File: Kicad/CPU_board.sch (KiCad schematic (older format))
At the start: 2 parts

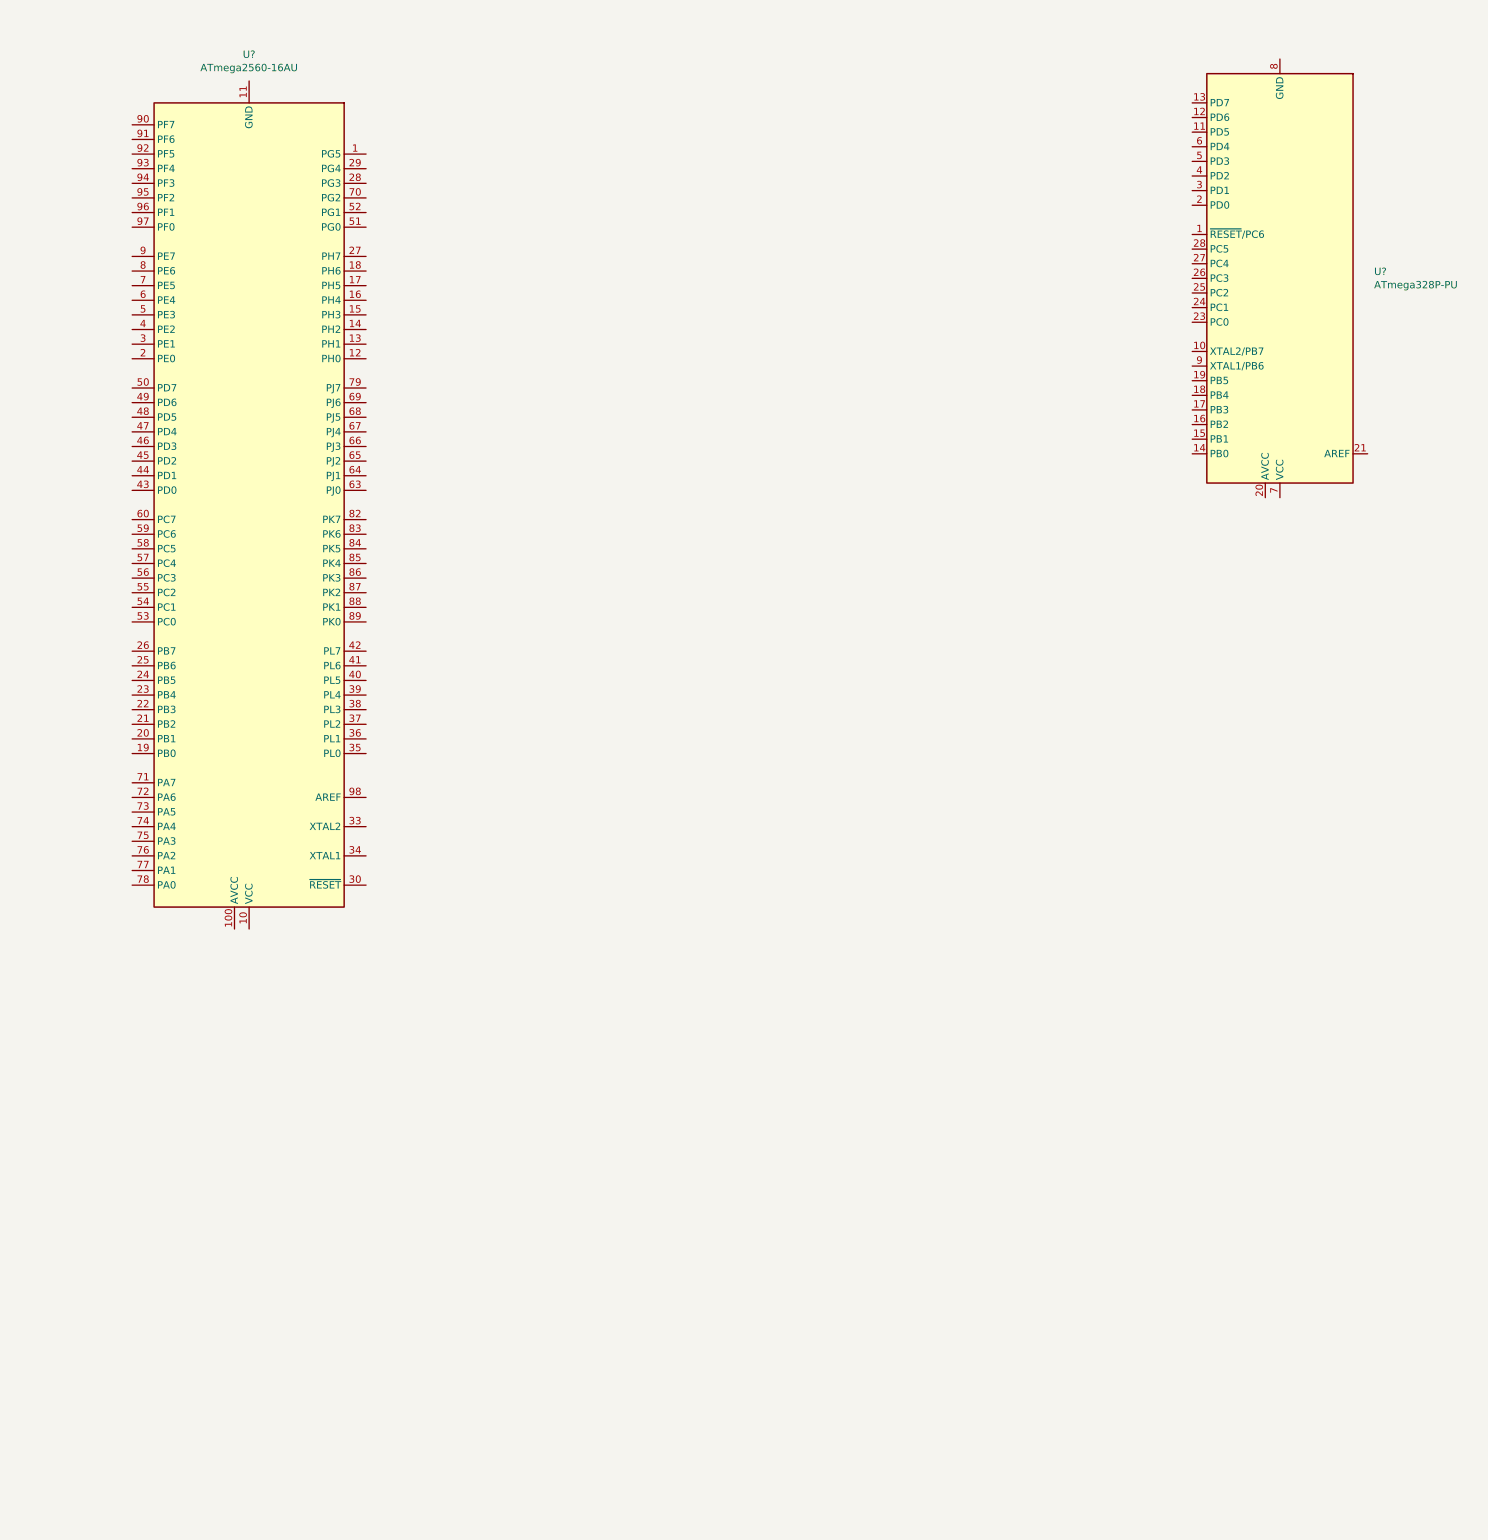
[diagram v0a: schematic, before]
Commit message: supprimé :        Kicad/CPU_board-cache.lib 	modifié :         Kicad/CPU_board.pro 	modifié :         Kicad/CPU_board.sch 	supprimé :        Kicad/CPU_board.sch-bak 	supprimé :        Kicad/Main_board-cache.lib 	modifié :         Kicad/Main_board.sch 	supprimé :        Kicad/Screen_board-cache.lib 	supprimé :        Kicad/Screen_board-rescue.dcm 	supprimé :        Kicad/Screen_board-rescue.lib 	supprimé :        Kicad/Screen_board.pro 	supprimé :        Kicad/Screen_board.sch 	supprimé :        Kicad/Screen_board.sch-bak
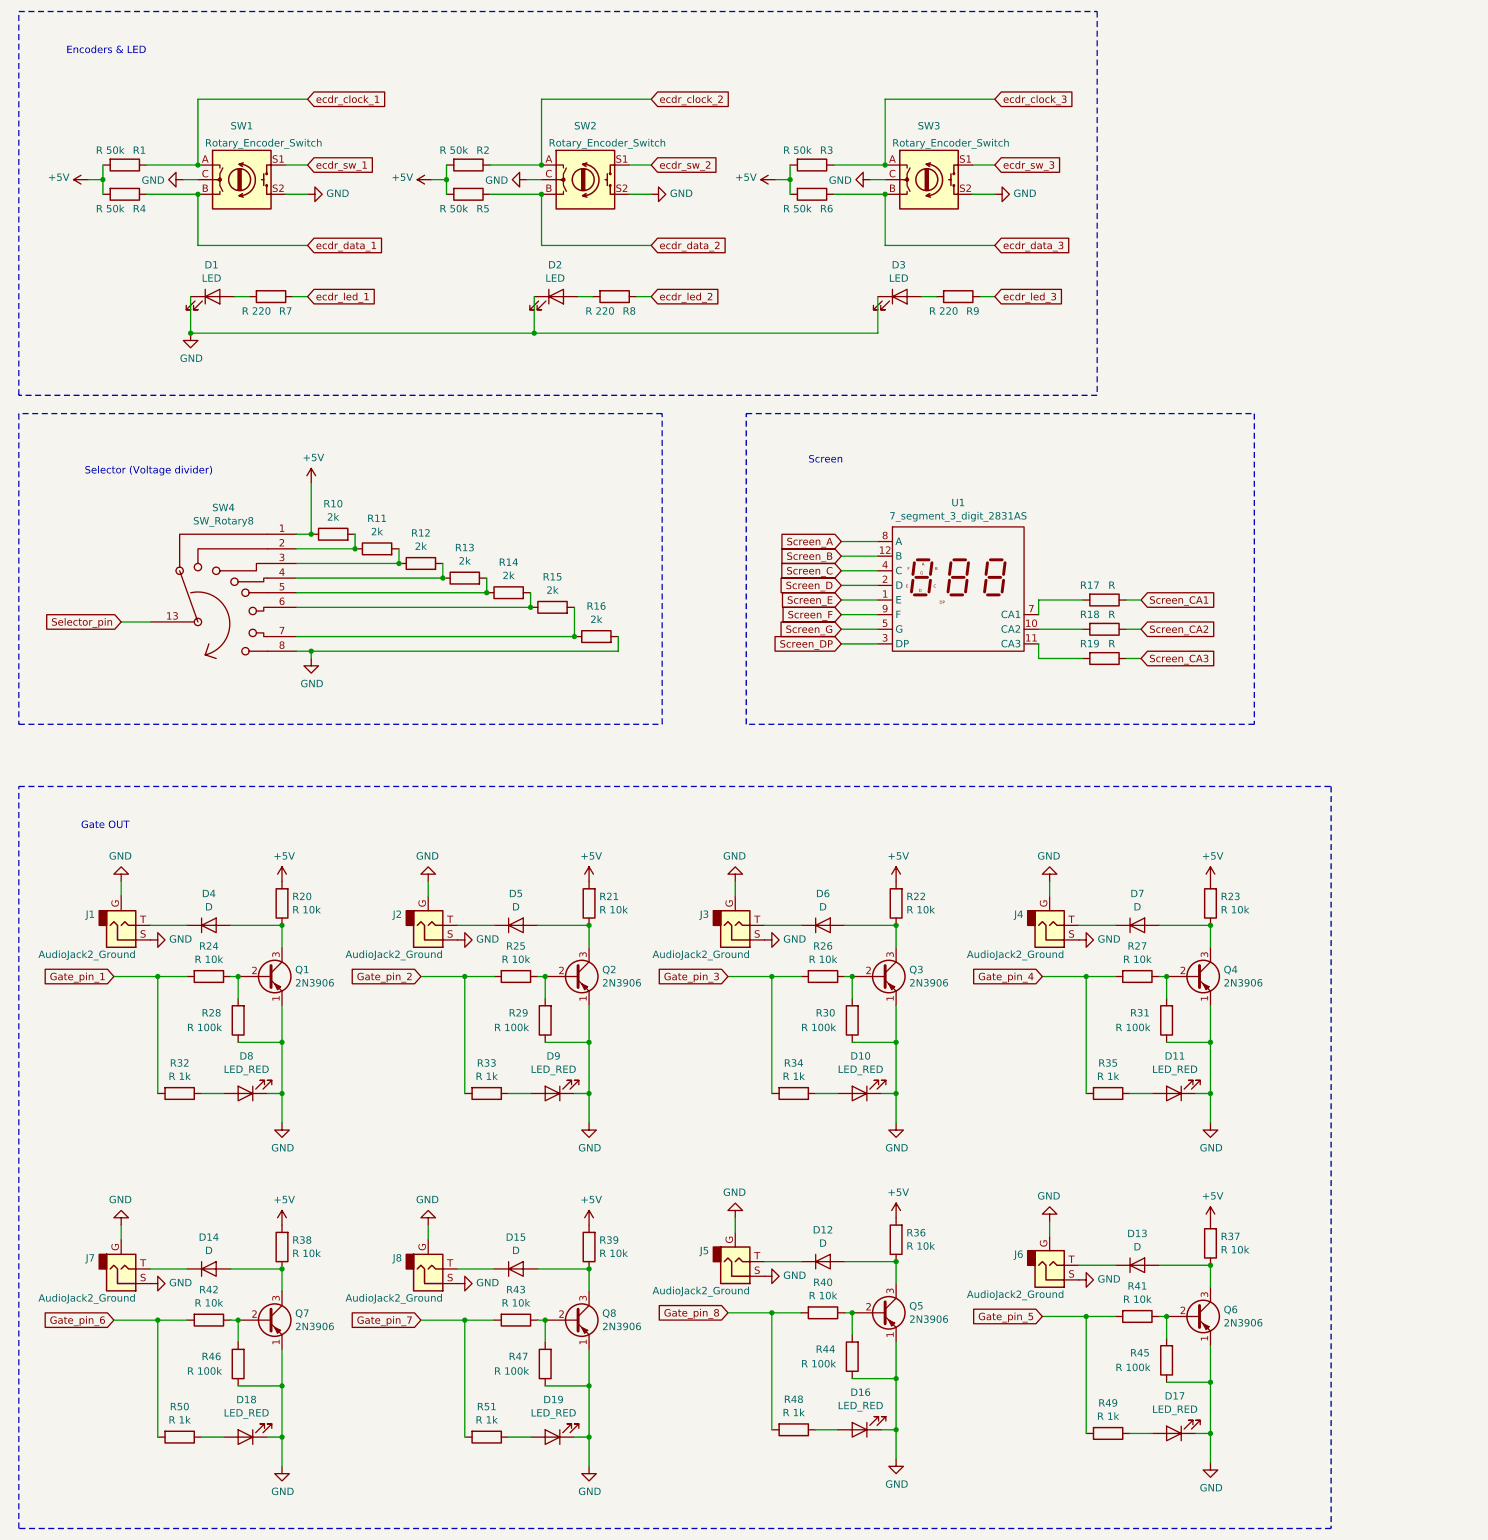
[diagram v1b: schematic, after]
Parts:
- removed U?: ATmega328P-PU, Package_DIP:DIP-28_W7.62mm, symbol MCU_Microchip_ATmega:ATmega328P-PU
- removed U?: ATmega2560-16AU, Package_QFP:TQFP-100_14x14mm_P0.5mm, symbol MCU_Microchip_ATmega:ATmega2560-16AU
- added D1, D2, D3: LED, symbol Device:LED
- added D10, D11, D16, D17, D18, D19, D8, D9: LED_RED, symbol Device:LED
- added D12, D13, D14, D15, D4, D5, D6, D7: D, symbol Device:D
- added J1, J2, J3, J4, J5, J6, J7, J8: AudioJack2_Ground, symbol Connector:AudioJack2_Ground
- added Q1, Q2, Q3, Q4, Q5, Q6, Q7, Q8: 2N3906, Package_TO_SOT_THT:TO-92_Inline, symbol Transistor_BJT:2N3906
- added R1, R2, R3, R4, R5, R6: R 50k, symbol Device:R
- added R10, R11, R12, R13, R14, R15, R16: 2k, symbol Device:R
- added R17, R18, R19: R, symbol Device:R
- added R20, R21, R22, R23, R24, R25, R26, R27, R36, R37, R38, R39, R40, R41, R42, R43: R 10k, symbol Device:R
- added R28, R29, R30, R31, R44, R45, R46, R47: R 100k, symbol Device:R
- added R32, R33, R34, R35, R48, R49, R50, R51: R 1k, symbol Device:R
- added R7, R8, R9: R 220, symbol Device:R
- added SW1, SW2, SW3: Rotary_Encoder_Switch, symbol Device:Rotary_Encoder_Switch
- added SW4: SW_Rotary8, symbol 00_Mes_symboles:SW_Rotary8-SW_Rotary_8
- added U1: 7_segment_3_digit_2831AS, Display_7Segment_3digit, symbol 00_Mes_symboles:7_segment_3_digit_2831AS-7_segments
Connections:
- new net: Q1.2 (B), R24.1, R28.2
- new net: D4.2 (A), Q1.3 (C), R20.1
- new net: D4.1 (K), J1.T
- new net: D5.2 (A), Q2.3 (C), R21.1
- new net: D9.2 (A), R33.1
- new net: Q2.2 (B), R25.1, R29.2
- new net: D5.1 (K), J2.T
- new net: D6.2 (A), Q3.3 (C), R22.1
- new net: D10.2 (A), R34.1
- new net: Q3.2 (B), R26.1, R30.2
- new net: D6.1 (K), J3.T
- new net: D7.2 (A), Q4.3 (C), R23.1
- new net: D11.2 (A), R35.1
- new net: Q4.2 (B), R27.1, R31.2
- new net: D7.1 (K), J4.T
- new net: D13.2 (A), Q6.3 (C), R37.1
- new net: D17.2 (A), R49.1
- new net: Q6.2 (B), R41.1, R45.2
- new net: D13.1 (K), J6.T
- new net: D14.2 (A), Q7.3 (C), R38.1
- new net: D18.2 (A), R50.1
- new net: Q7.2 (B), R42.1, R46.2
- new net: D14.1 (K), J7.T
- new net: D15.2 (A), Q8.3 (C), R39.1
- new net: D19.2 (A), R51.1
- new net: Q8.2 (B), R43.1, R47.2
- new net: D15.1 (K), J8.T
- new net: D12.2 (A), Q5.3 (C), R36.1
- new net: D16.2 (A), R48.1
- new net: Q5.2 (B), R40.1, R44.2
- new net: D12.1 (K), J5.T
- new net: R10.2, R11.1, SW4.2
- new net: R11.2, R12.1, SW4.3
- new net: R12.2, R13.1, SW4.4
- new net: R13.2, R14.1, SW4.5
- new net: R14.2, R15.1, SW4.6
- new net: R15.2, R16.1, SW4.7
- new net: D8.2 (A), R32.1
- new net: R18.2, U1.10 (CA2)
- new net: R19.2, U1.11 (CA3)
- new net: R17.2, U1.7 (CA1)
- new net: D1.2 (A), R7.2
- new net: D2.2 (A), R8.2
- new net: D3.2 (A), R9.2
- new net +5V: R1.2, R10.1, R2.2, R20.2, R21.2, R22.2, R23.2, R3.2, R36.2, R37.2, R38.2, R39.2, R4.2, R5.2, R6.2, SW4.1
- new net GND: D1.1 (K), D10.1 (K), D11.1 (K), D16.1 (K), D17.1 (K), D18.1 (K), D19.1 (K), D2.1 (K), D3.1 (K), D8.1 (K), D9.1 (K), J1.G, J1.S, J2.G, J2.S, J3.G, J3.S, J4.G, J4.S, J5.G, J5.S, J6.G, J6.S, J7.G, J7.S, J8.G, J8.S, Q1.1 (E), Q2.1 (E), Q3.1 (E), Q4.1 (E), Q5.1 (E), Q6.1 (E), Q7.1 (E), Q8.1 (E), R16.2, R28.1, R29.1, R30.1, R31.1, R44.1, R45.1, R46.1, R47.1, SW1.C, SW1.S2, SW2.C, SW2.S2, SW3.C, SW3.S2, SW4.8
- new net Gate_pin_1: R24.2, R32.2
- new net Gate_pin_2: R25.2, R33.2
- new net Gate_pin_3: R26.2, R34.2
- new net Gate_pin_4: R27.2, R35.2
- new net Gate_pin_5: R41.2, R49.2
- new net Gate_pin_6: R42.2, R50.2
- new net Gate_pin_7: R43.2, R51.2
- new net Gate_pin_8: R40.2, R48.2
- new net Screen_A: U1.8 (A)
- new net Screen_B: U1.12 (B)
- new net Screen_C: U1.4 (C)
- new net Screen_CA1: R17.1
- new net Screen_CA2: R18.1
- new net Screen_CA3: R19.1
- new net Screen_D: U1.2 (D)
- new net Screen_DP: U1.3 (DP)
- new net Screen_E: U1.1 (E)
- new net Screen_F: U1.9 (F)
- new net Screen_G: U1.5 (G)
- new net Selector_pin: SW4.13
- new net ecdr_clock_1: R1.1, SW1.A
- new net ecdr_clock_2: R2.1, SW2.A
- new net ecdr_clock_3: R3.1, SW3.A
- new net ecdr_data_1: R4.1, SW1.B
- new net ecdr_data_2: R5.1, SW2.B
- new net ecdr_data_3: R6.1, SW3.B
- new net ecdr_led_1: R7.1
- new net ecdr_led_2: R8.1
- new net ecdr_led_3: R9.1
- new net ecdr_sw_1: SW1.S1
- new net ecdr_sw_2: SW2.S1
- new net ecdr_sw_3: SW3.S1
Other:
- note added: "Encoders & LED"
- note added: "Gate OUT"
- note added: "Screen"
- note added: "Selector (Voltage divider)"
